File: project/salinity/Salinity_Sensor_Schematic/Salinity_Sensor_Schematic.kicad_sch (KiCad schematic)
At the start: 12 parts, among them U1 MCP6L01, U2 LM555

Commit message: salinitysschem2
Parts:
- C3, C4: value C -> 1n
- R1, R4: value R_US -> 15k
- R5: value R_US -> 10k
- R6: value R_US -> 1k
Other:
- note removed: "First resistor in voltage divider label as Rprobe"
- moved on the sheet: R1
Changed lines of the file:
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@@
     (stroke (width 0) (type default))
   )
-  (wire (pts (xy 97.79 66.04) (xy 100.33 66.04))
+  (wire (pts (xy 95.25 66.04) (xy 100.33 66.04))
     (stroke (width 0) (type default))
   )
@@
     (stroke (width 0) (type default))
   )
-  (wire (pts (xy 73.66 66.04) (xy 90.17 66.04))
+  (wire (pts (xy 73.66 66.04) (xy 87.63 66.04))
     (stroke (width 0) (type default))
   )
@@
   (wire (pts (xy 58.42 53.34) (xy 58.42 59.69))
     (stroke (width 0) (type default))
-  )
-  (text "First resistor in voltage divider label as Rprobe" (at 123.19 101.6 0)
-    (effects (font (size 1.27 1.27)) (justify left bottom))
   )
   (text "AC out" (at 152.4 71.12 0)
@@
       (effects (font (size 1.27 1.27)))
     )
-    (property "Value" "R_US" (at 140.97 74.93 90)
-      (effects (font (size 1.27 1.27)) hide)
+    (property "Value" "1k" (at 140.97 81.28 90)
+      (effects (font (size 1.27 1.27)))
     )
     (property "Footprint" "" (at 141.224 77.724 90)
@@
       (effects (font (size 1.27 1.27)) (justify left))
     )
-    (property "Value" "R_US" (at 128.27 83.82 0)
-      (effects (font (size 1.27 1.27)) (justify left) hide)
+    (property "Value" "10k" (at 128.27 83.82 0)
+      (effects (font (size 1.27 1.27)) (justify left))
     )
     (property "Footprint" "" (at 126.746 82.804 90)
@@
     )
   )
-  (symbol (lib_id "Device:R_US") (at 93.98 66.04 90) (unit 1)
-    (in_bom yes) (on_board yes) (dnp no)
-    (property "Reference" "R1" (at 93.98 63.5 90)
-      (effects (font (size 1.27 1.27)))
-    )
-    (property "Value" "R_US" (at 93.98 62.23 90)
-      (effects (font (size 1.27 1.27)) hide)
-    )
-    (property "Footprint" "" (at 94.234 65.024 90)
-      (effects (font (size 1.27 1.27)) hide)
-    )
-    (property "Datasheet" "~" (at 93.98 66.04 0)
+  (symbol (lib_id "Device:R_US") (at 91.44 66.04 90) (unit 1)
+    (in_bom yes) (on_board yes) (dnp no)
+    (property "Reference" "R1" (at 91.44 63.5 90)
+      (effects (font (size 1.27 1.27)))
+    )
+    (property "Value" "15k" (at 91.44 68.58 90)
+      (effects (font (size 1.27 1.27)))
+    )
+    (property "Footprint" "" (at 91.694 65.024 90)
+      (effects (font (size 1.27 1.27)) hide)
+    )
+    (property "Datasheet" "~" (at 91.44 66.04 0)
       (effects (font (size 1.27 1.27)) hide)
     )
@@
       (effects (font (size 1.27 1.27)))
     )
-    (property "Value" "R_US" (at 107.95 62.23 90)
-      (effects (font (size 1.27 1.27)) hide)
+    (property "Value" "15k" (at 107.95 68.58 90)
+      (effects (font (size 1.27 1.27)))
     )
     (property "Footprint" "" (at 108.204 65.024 90)
@@
       (effects (font (size 1.27 1.27)) (justify left))
     )
-    (property "Value" "C" (at 119.38 77.47 0)
-      (effects (font (size 1.27 1.27)) (justify left) hide)
+    (property "Value" "1n" (at 116.84 73.66 0)
+      (effects (font (size 1.27 1.27)) (justify left))
     )
     (property "Footprint" "" (at 116.5352 80.01 0)
@@
   (symbol (lib_id "Device:C") (at 130.81 57.15 90) (unit 1)
     (in_bom yes) (on_board yes) (dnp no)
-    (property "Reference" "C3" (at 130.81 52.07 90)
-      (effects (font (size 1.27 1.27)))
-    )
-    (property "Value" "C" (at 130.81 52.07 90)
-      (effects (font (size 1.27 1.27)) hide)
+    (property "Reference" "C3" (at 133.35 53.34 90)
+      (effects (font (size 1.27 1.27)))
+    )
+    (property "Value" "1n" (at 130.81 52.07 90)
+      (effects (font (size 1.27 1.27)))
     )
     (property "Footprint" "" (at 134.62 56.1848 0)

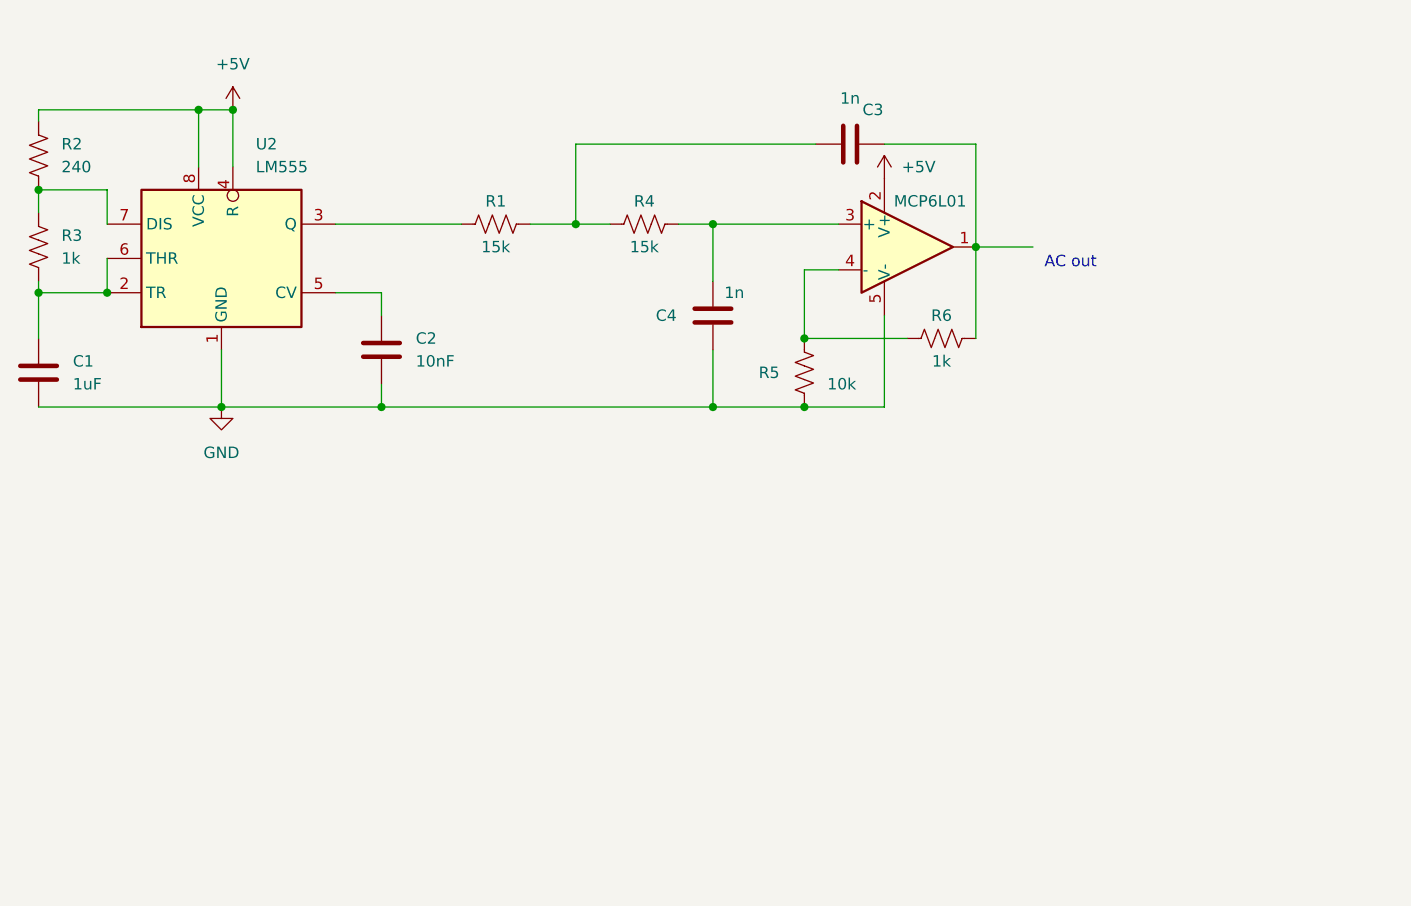
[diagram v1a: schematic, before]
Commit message: surface control + kicad salinity updates
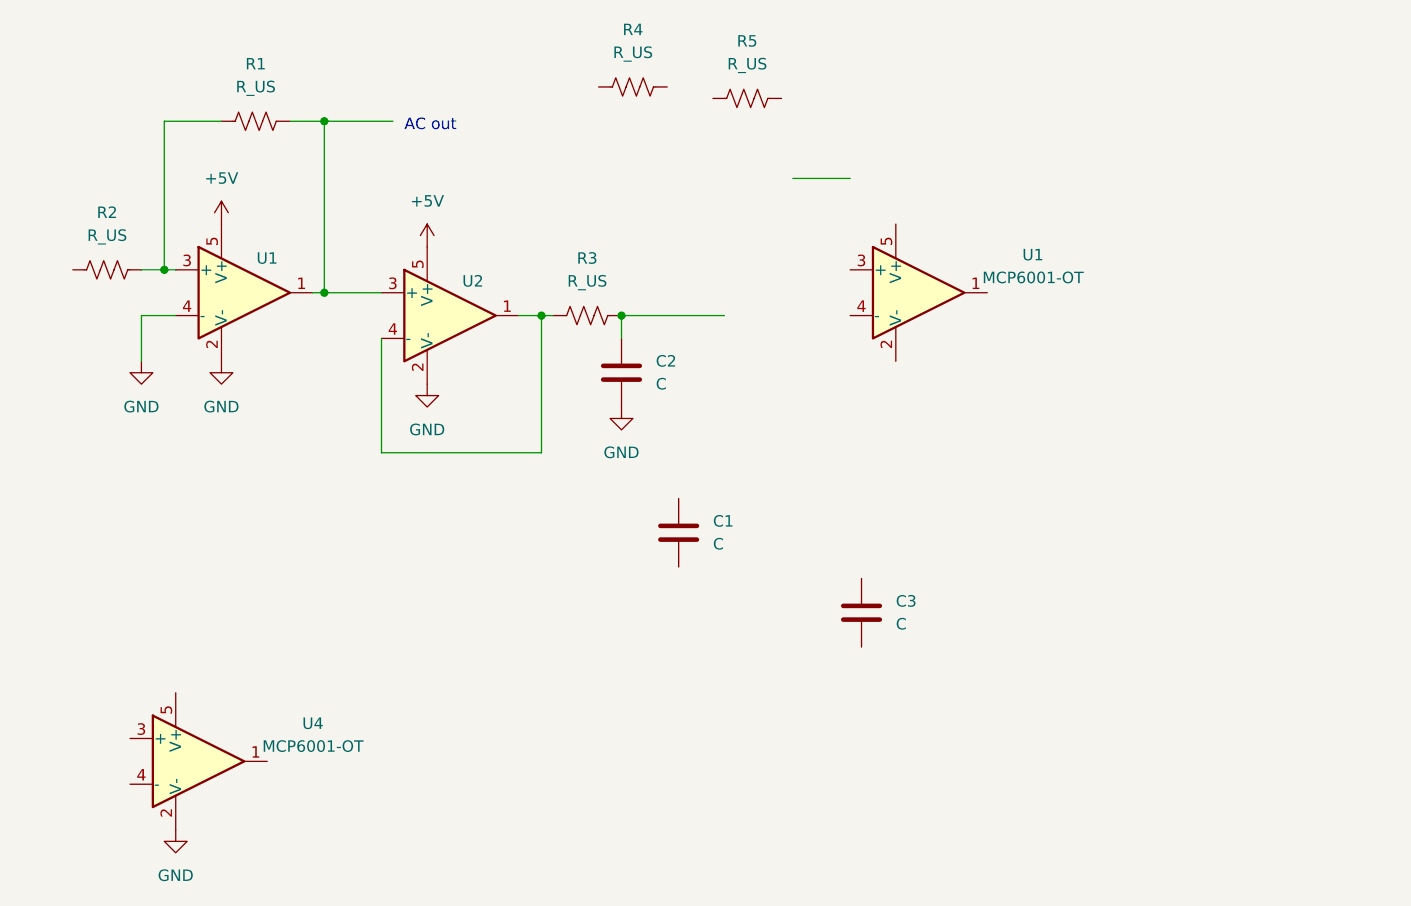
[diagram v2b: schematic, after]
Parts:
- removed C4: 1n, symbol Device:C
- removed R6: 1k, symbol Device:R_US
- removed U1: MCP6L01, Package_TO_SOT_SMD:SOT-23-5, symbol Amplifier_Operational:MCP6L01Rx-xOT
- removed U2: LM555, Package_DIP:DIP-8_W7.62mm, symbol Timer:SE555P
- added U1, U2, U4: MCP6001-OT, Package_TO_SOT_SMD:SOT-23-5, symbol Amplifier_Operational:MCP6001-OT
- added U3: U1, Package_TO_SOT_SMD:SOT-23-5, symbol Amplifier_Operational:MCP6001-OT
- C1: value 1uF -> C
- C2: value 10nF -> C
- C3: value 1n -> C
- R1, R4: value 15k -> R_US
- R2: value 240 -> R_US
- R3: value 1k -> R_US
- R5: value 10k -> R_US
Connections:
- net +5V: now also U2.5 (V+), U3.5 (V+); no longer R2.1
- net GND: now also U2.2 (V-), U3.2 (V-), U3.4 (-), U4.2 (V-); no longer C1.2, R5.2
- net at C2.1: now also R3.2
- net at R3.1: now also U2.1, U2.4 (-); no longer R2.2
- net at C1.1: no longer R3.2
- net at R1.1: now also R2.1, U3.3 (+)
- new net: R1.2, U2.3 (+), U3.1
- now unconnected: C3.1, R4.1

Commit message: kiCad Salinity
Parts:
- renumbered C2 to C1, C1 to C2, U1 to U3
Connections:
- net +5V: now also U3.5 (V+), U4.5 (V+)
- net GND: now also C2.2, C3.2, U3.2 (V-)
- net at C1.1, R3.2: now also U3.3 (+)
- net at C3.1: now also R5.2
- net at C2.1: now also R4.2, U4.3 (+)
- net at U4.1: now also R5.1
- net at U4.4 (-): now also R2.2
- net at R4.1: now also U3.1, U3.4 (-)
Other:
- company: (none) -> E80
- title: (none) -> Salinity Sensor
- moved on the sheet: C2, C3, R4, R5, U3, U4
